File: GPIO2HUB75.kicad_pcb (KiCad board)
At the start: 2 copper layers, 30.2 x 59.5 mm, 7 parts, among them J2 Conn_02x20_Odd_Even_MountingP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, J3 Conn_02x08_Top_Bottom, J4 Conn_02x05_Odd_Even, J5 Conn_02x03_Odd_Even, M1 Fan_3pin

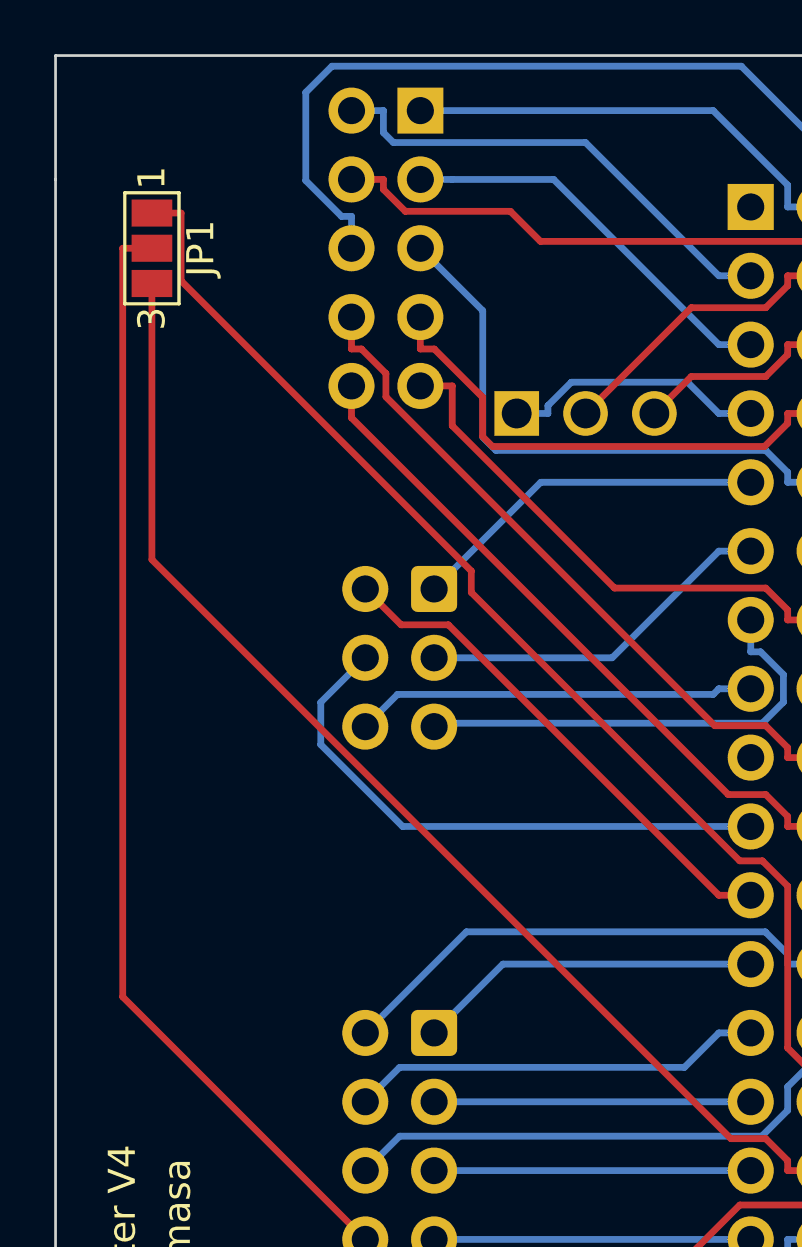
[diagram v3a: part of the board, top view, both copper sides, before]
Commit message: added tilt sensor
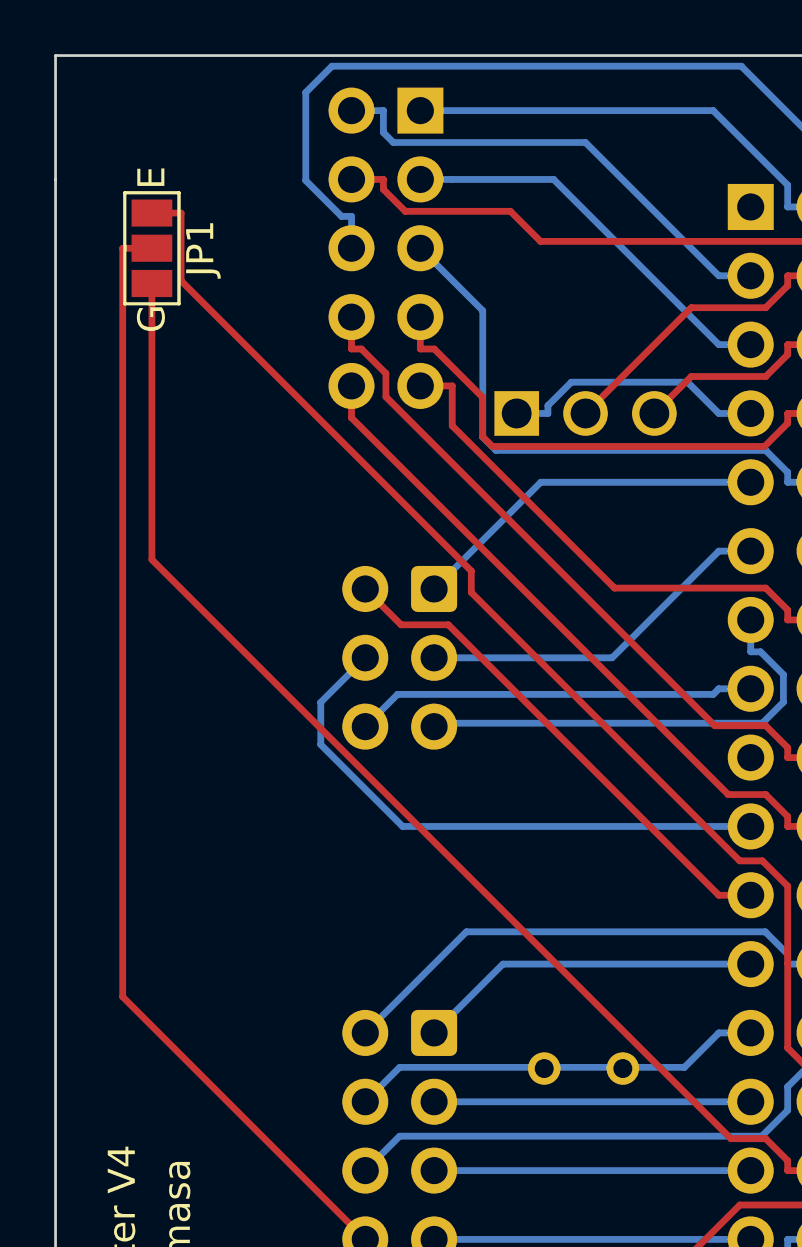
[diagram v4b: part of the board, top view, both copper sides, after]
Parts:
- added S1: CW1300-1, Tilt Sensor:CW13001, B.Cu at (156.8, 92.8)
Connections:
- J2 pad 1: unconnected-(J2-Pin_1-Pad1) -> Net-(J2-Pin_1)
- J2 pad 12: Net-(J2-Pin_12) -> unconnected-(J2-Pin_12-Pad12)
- J4 pad 2: Net-(J2-Pin_3) -> Net-(J2-Pin_1)
- J4 pad 4: Net-(J2-Pin_12) -> Net-(J2-Pin_3)
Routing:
- net Net-(J2-Pin_3): track 17.7 -> 49.1 mm
- net Net-(J2-Pin_12): track 31.3 -> 0.00 mm
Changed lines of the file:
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@@
   (net 2 "Net-(J2-Pin_39)")
   (net 3 "Net-(J2-Pin_7)")
-  (net 4 "unconnected-(J2-Pin_1-Pad1)")
+  (net 4 "Net-(J2-Pin_1)")
   (net 5 "Net-(J2-Pin_23)")
   (net 6 "Net-(J2-Pin_24)")
@@
   (net 27 "Net-(J2-Pin_10)")
   (net 28 "Net-(J2-Pin_11)")
-  (net 29 "Net-(J2-Pin_12)")
+  (net 29 "unconnected-(J2-Pin_12-Pad12)")
   (net 30 "Net-(J2-Pin_13)")
   (net 31 "Net-(J2-Pin_14)")
@@
   (net 40 "Net-(BZ1-+)")
   (net 41 "unconnected-(J2-Pin_17-Pad17)")
+  (net 42 "unconnected-(S1-Pad1)")
+  (net 43 "unconnected-(S1-Pad2)")
   (footprint "Jumper:SolderJumper-3_P1.3mm_Open_Pad1.0x1.5mm_NumberLabels" (layer "F.Cu")
     (at 139.446 62.484 -90)
@@
         (effects (font (size 1 1) (thickness 0.15)))
     )
-    (fp_text user "1" (at -2.6 0 90) (layer "F.SilkS")
+    (fp_text user "E" (at -2.6 0 90) (layer "F.SilkS")
         (effects (font (size 1 1) (thickness 0.15)))
     )
-    (fp_text user "3" (at 2.6 0 90) (layer "F.SilkS")
+    (fp_text user "G" (at 2.6 0 90) (layer "F.SilkS")
         (effects (font (size 1 1) (thickness 0.15)))
     )
@@
     (pad "3" smd rect (at 1.3 0 270) (size 1 1.5) (layers "F.Cu" "F.Mask")
       (net 38 "Net-(J2-Pin_30)") (pinfunction "B") (pintype "passive"))
+  )
+  (footprint "Tilt Sensor:CW13001" (layer "B.Cu")
+    (at 156.824 92.754 180)
+    (descr "CW1300-1-2")
+    (tags "Switch")
+    (property "Farnell Part Number" "")
+    (property "Farnell Price/Stock" "")
+    (property "Height" "10.2")
+    (property "Manufacturer_Name" "Assemtech")
+    (property "Manufacturer_Part_Number" "CW1300-1")
+    (property "Sheetfile" "GPIO2HUB75.kicad_sch")
+    (property "Sheetname" "")
+    (property "ki_description" "15 , 0.25 A, 60V, Non-Mercury Tilt Switch")
+    (attr through_hole)
+    (fp_text reference "S1" (at 0.575 0.425) (layer "B.SilkS")
+        (effects (font (size 1.27 1.27) (thickness 0.254)) (justify mirror))
+    )
+    (fp_text value "CW1300-1" (at 0.575 0.425) (layer "B.SilkS") hide
+        (effects (font (size 1.27 1.27) (thickness 0.254)) (justify mirror))
+    )
+    (fp_text user "${REFERENCE}" (at 0.575 0.425) (layer "B.Fab")
+        (effects (font (size 1.27 1.27) (thickness 0.254)) (justify mirror))
+    )
+    (fp_line (start 0 3.1) (end 0 3.1)
+      (stroke (width 0.2) (type solid)) (layer "B.SilkS"))
+    (fp_line (start 0 3.1) (end 0 3.1)
+      (stroke (width 0.2) (type solid)) (layer "B.SilkS"))
+    (fp_line (start 0 3.2) (end 0 3.2)
+      (stroke (width 0.2) (type solid)) (layer "B.SilkS"))
+    (fp_arc (start 0 3.1) (mid 0.05 3.15) (end 0 3.2)
+      (stroke (width 0.2) (type solid)) (layer "B.SilkS"))
+    (fp_arc (start 0 3.1) (mid 0.05 3.15) (end 0 3.2)
+      (stroke (width 0.2) (type solid)) (layer "B.SilkS"))
+    (fp_arc (start 0 3.2) (mid -0.05 3.15) (end 0 3.1)
+      (stroke (width 0.2) (type solid)) (layer "B.SilkS"))
+    (fp_line (start -3.35 -3.35) (end -3.35 4.2)
+      (stroke (width 0.1) (type solid)) (layer "B.CrtYd"))
+    (fp_line (start -3.35 4.2) (end 4.5 4.2)
+      (stroke (width 0.1) (type solid)) (layer "B.CrtYd"))
+    (fp_line (start 4.5 -3.35) (end -3.35 -3.35)
+      (stroke (width 0.1) (type solid)) (layer "B.CrtYd"))
+    (fp_line (start 4.5 4.2) (end 4.5 -3.35)
+      (stroke (width 0.1) (type solid)) (layer "B.CrtYd"))
+    (fp_line (start -2.35 0) (end -2.35 0)
+      (stroke (width 0.2) (type solid)) (layer "B.Fab"))
+    (fp_line (start 2.35 0) (end 2.35 0)
+      (stroke (width 0.2) (type solid)) (layer "B.Fab"))
+    (fp_arc (start -2.35 0) (mid 0 -2.35) (end 2.35 0)
+      (stroke (width 0.2) (type solid)) (layer "B.Fab"))
+    (fp_arc (start 2.35 0) (mid 0 2.35) (end -2.35 0)
+      (stroke (width 0.2) (type solid)) (layer "B.Fab"))
+    (pad "1" thru_hole circle (at 0 0 180) (size 1.2 1.2) (drill 0.7) (layers "*.Cu" "*.Mask")
+      (net 42 "unconnected-(S1-Pad1)") (pinfunction "1") (pintype "passive"))
+    (pad "2" thru_hole circle (at 2.9 0 180) (size 1.2 1.2) (drill 0.7) (layers "*.Cu" "*.Mask")
+      (net 43 "unconnected-(S1-Pad2)") (pinfunction "2") (pintype "passive"))
+    (model "C:/Users/Admin/Downloads/LIB_CW1300-1/CW1300-1/3D/CW1300-1.stp"
+      (offset (xyz 0 2.5 3))
+      (scale (xyz 1 1 1))
+      (rotate (xyz 90 0 0))
+    )
   )
   (footprint "Buzzer_Beeper:MagneticBuzzer_Kingstate_KCG0601" (layer "B.Cu")
@@
       (net 22 "Net-(J2-Pin_2)") (pinfunction "Pin_1") (pintype "passive"))
     (pad "2" thru_hole oval (at 2.54 0 180) (size 1.7 1.7) (drill 1) (layers "*.Cu" "*.Mask")
-      (net 23 "Net-(J2-Pin_3)") (pinfunction "Pin_2") (pintype "passive"))
+      (net 4 "Net-(J2-Pin_1)") (pinfunction "Pin_2") (pintype "passive"))
     (pad "3" thru_hole oval (at 0 -2.54 180) (size 1.7 1.7) (drill 1) (layers "*.Cu" "*.Mask")
       (net 24 "Net-(J2-Pin_5)") (pinfunction "Pin_3") (pintype "passive"))
     (pad "4" thru_hole oval (at 2.54 -2.54 180) (size 1.7 1.7) (drill 1) (layers "*.Cu" "*.Mask")
-      (net 29 "Net-(J2-Pin_12)") (pinfunction "Pin_4") (pintype "passive"))
+      (net 23 "Net-(J2-Pin_3)") (pinfunction "Pin_4") (pintype "passive"))
     (pad "5" thru_hole oval (at 0 -5.08 180) (size 1.7 1.7) (drill 1) (layers "*.Cu" "*.Mask")
       (net 27 "Net-(J2-Pin_10)") (pinfunction "Pin_5") (pintype "passive"))
@@
       (stroke (width 0.1) (type solid)) (layer "B.Fab"))
     (pad "1" thru_hole rect (at 0 0 180) (size 1.7 1.7) (drill 1) (layers "*.Cu" "*.Mask")
-      (net 4 "unconnected-(J2-Pin_1-Pad1)") (pinfunction "Pin_1") (pintype "passive"))
+      (net 4 "Net-(J2-Pin_1)") (pinfunction "Pin_1") (pintype "passive"))
     (pad "2" thru_hole oval (at -2.54 0 180) (size 1.7 1.7) (drill 1) (layers "*.Cu" "*.Mask")
       (net 22 "Net-(J2-Pin_2)") (pinfunction "Pin_2") (pintype "passive"))
@@
       (net 28 "Net-(J2-Pin_11)") (pinfunction "Pin_11") (pintype "passive"))
     (pad "12" thru_hole oval (at -2.54 -12.7 180) (size 1.7 1.7) (drill 1) (layers "*.Cu" "*.Mask")
-      (net 29 "Net-(J2-Pin_12)") (pinfunction "Pin_12") (pintype "passive"))
+      (net 29 "unconnected-(J2-Pin_12-Pad12)") (pinfunction "Pin_12") (pintype "passive"))
     (pad "13" thru_hole oval (at 0 -15.24 180) (size 1.7 1.7) (drill 1) (layers "*.Cu" "*.Mask")
       (net 30 "Net-(J2-Pin_13)") (pinfunction "Pin_13") (pintype "passive"))
@@
   (segment (start 160.1602 57.404) (end 162.9071 60.1509) (width 0.25) (layer "B.Cu") (net 22))
   (segment (start 164.084 60.96) (end 162.9071 60.96) (width 0.25) (layer "B.Cu") (net 22))
+  (segment (start 165.277 71.6559) (end 164.4498 72.4831) (width 0.25) (layer "F.Cu") (net 23))
+  (segment (start 148.7979 61.1209) (end 152.6768 61.1209) (width 0.25) (layer "F.Cu") (net 23))
+  (segment (start 146.812 59.944) (end 147.9889 59.944) (width 0.25) (layer "F.Cu") (net 23))
+  (segment (start 147.9889 60.3119) (end 148.7979 61.1209) (width 0.25) (layer "F.Cu") (net 23))
+  (segment (start 147.9889 59.944) (end 147.9889 60.3119) (width 0.25) (layer "F.Cu") (net 23))
+  (segment (start 164.4498 72.4831) (end 164.084 72.4831) (width 0.25) (layer "F.Cu") (net 23))
+  (segment (start 152.6768 61.1209) (end 153.7859 62.23) (width 0.25) (layer "F.Cu") (net 23))
+  (segment (start 165.277 62.9734) (end 165.277 71.6559) (width 0.25) (layer "F.Cu") (net 23))
+  (segment (start 164.084 73.66) (end 164.084 72.4831) (width 0.25) (layer "F.Cu") (net 23))
+  (segment (start 153.7859 62.23) (end 164.5336 62.23) (width 0.25) (layer "F.Cu") (net 23))
+  (segment (start 164.5336 62.23) (end 165.277 62.9734) (width 0.25) (layer "F.Cu") (net 23))
   (segment (start 161.544 63.5) (end 160.3671 63.5) (width 0.25) (layer "B.Cu") (net 23))
   (segment (start 147.9889 58.2132) (end 148.3566 58.5809) (width 0.25) (layer "B.Cu") (net 23))
@@
   (segment (start 161.544 73.66) (end 160.3671 73.66) (width 0.25) (layer "B.Cu") (net 28))
   (segment (start 149.86 77.597) (end 156.4301 77.597) (width 0.25) (layer "B.Cu") (net 28))
-  (segment (start 165.277 71.6559) (end 164.4498 72.4831) (width 0.25) (layer "F.Cu") (net 29))
-  (segment (start 148.7979 61.1209) (end 152.6768 61.1209) (width 0.25) (layer "F.Cu") (net 29))
-  (segment (start 146.812 59.944) (end 147.9889 59.944) (width 0.25) (layer "F.Cu") (net 29))
-  (segment (start 147.9889 60.3119) (end 148.7979 61.1209) (width 0.25) (layer "F.Cu") (net 29))
-  (segment (start 147.9889 59.944) (end 147.9889 60.3119) (width 0.25) (layer "F.Cu") (net 29))
-  (segment (start 164.4498 72.4831) (end 164.084 72.4831) (width 0.25) (layer "F.Cu") (net 29))
-  (segment (start 152.6768 61.1209) (end 153.7859 62.23) (width 0.25) (layer "F.Cu") (net 29))
-  (segment (start 165.277 62.9734) (end 165.277 71.6559) (width 0.25) (layer "F.Cu") (net 29))
-  (segment (start 164.084 73.66) (end 164.084 72.4831) (width 0.25) (layer "F.Cu") (net 29))
-  (segment (start 153.7859 62.23) (end 164.5336 62.23) (width 0.25) (layer "F.Cu") (net 29))
-  (segment (start 164.5336 62.23) (end 165.277 62.9734) (width 0.25) (layer "F.Cu") (net 29))
   (segment (start 162.7505 78.2176) (end 161.9098 77.3769) (width 0.25) (layer "B.Cu") (net 30))
   (segment (start 149.86 80.137) (end 149.987 80.01) (width 0.25) (layer "B.Cu") (net 30))

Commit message: version 5
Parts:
- removed J2: Conn_02x20_Odd_Even_MountingPin, Connector_PinSocket_2.54mm:PinSocket_2x20_P2.54mm_Vertical
- added RPiGPIO1: CONN_02X20, Connector_PinSocket_2.54mm:PinSocket_2x20_P2.54mm_Vertical, B.Cu at (164.0, 110.2)
- E: renamed from JP1; value SolderJumper_3_Open -> Data E
- GPIO1: renamed from J4; value Conn_02x05_Odd_Even -> 02x04; footprint Connector_PinHeader_2.54mm:PinHeader_2x05_P2.54mm_Horizontal -> Connector_PinHeader_2.54mm:PinHeader_2x04_P2.54mm_Horizontal
- HUB1: renamed from J3; value Conn_02x08_Top_Bottom -> Conn_02x08
- IO1: renamed from J5; value Conn_02x03_Odd_Even -> 02x03
- M1: value Fan_3pin -> Noctua
- S1: value CW1300-1 -> CW1300
- moved GPIO1 2.55 mm to (149.1, 59.9)
- moved M1 2.48 mm to (152.8, 71.1)
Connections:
- BZ1 pad 1: Net-(BZ1--) -> BUZZ
- E pad 1: Net-(J2-Pin_28) -> GPIO15
- E pad 3: Net-(J2-Pin_30) -> Net-(BZ1-+)
- GPIO1 pad 1: Net-(J2-Pin_2) -> GPIO 2
- GPIO1 pad 2: Net-(J2-Pin_1) -> GPIO 26
- GPIO1 pad 3: Net-(J2-Pin_5) -> GPIO 3
- GPIO1 pad 4: Net-(J2-Pin_3) -> GPIO 6
- GPIO1 pad 5: Net-(J2-Pin_10) -> GPIO 13
- GPIO1 pad 6: Net-(J2-Pin_16) -> VCC
- GPIO1 pad 7: Net-(J2-Pin_8) -> GPIO 19
- GPIO1 pad 8: Net-(J2-Pin_18) -> Net-(BZ1-+)
- HUB1 pad 1: Net-(J2-Pin_23) -> R1
- HUB1 pad 10: Net-(J2-Pin_32) -> B
- HUB1 pad 11: Net-(J2-Pin_35) -> C
- HUB1 pad 12: Net-(J2-Pin_36) -> D
- HUB1 pad 13: Net-(J2-Pin_37) -> Clock
- HUB1 pad 14: Net-(J2-Pin_38) -> Net-(BZ1-+)
- HUB1 pad 15: Net-(J2-Pin_40) -> OE-
- HUB1 pad 16: Net-(J2-Pin_39) -> Strobe
- HUB1 pad 2: Net-(J2-Pin_24) -> G1
- HUB1 pad 3: Net-(J2-Pin_27) -> B1
- HUB1 pad 4: Net-(J2-Pin_25) -> Net-(BZ1-+)
- HUB1 pad 5: Net-(J2-Pin_29) -> R2
- HUB1 pad 6: Net-(J2-Pin_26) -> G2
- HUB1 pad 7: Net-(J2-Pin_31) -> B2
- HUB1 pad 9: Net-(J2-Pin_33) -> A
- IO1 pad 1: Net-(J2-Pin_9) -> IO1
- IO1 pad 2: Net-(J2-Pin_21) -> IO2
- IO1 pad 3: Net-(J2-Pin_11) -> IO3
- IO1 pad 4: Net-(J2-Pin_19) -> IO4
- IO1 pad 5: Net-(J2-Pin_13) -> IO5
- IO1 pad 6: Net-(J2-Pin_15) -> Net-(BZ1-+)
- M1 pad 1: Net-(J2-Pin_7) -> VCC
- M1 pad 2: Net-(J2-Pin_4) -> Net-(BZ1-+)
- M1 pad 3: Net-(J2-Pin_6) -> FAN
- S1 pad 1: unconnected-(S1-Pad1) -> TILT
- S1 pad 2: unconnected-(S1-Pad2) -> Net-(BZ1-+)
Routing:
- net Net-(BZ1-+): track 17.6 -> 97.6 mm
- net GPIO 2: track 0.00 -> 62.5 mm
- net GPIO 3: track 0.00 -> 57.1 mm
- net VCC: track 0.00 -> 52.8 mm
- net Net-(J2-Pin_3): track 49.1 -> 0.00 mm
- net Net-(J2-Pin_16): track 48.9 -> 0.00 mm
- net Net-(J2-Pin_30): track 44.4 -> 0.00 mm
- net Net-(J2-Pin_28): track 44.3 -> 0.00 mm
- net BUZZ: track 0.00 -> 39.2 mm
- net C: track 0.00 -> 37.6 mm
- net G1: track 0.00 -> 36.7 mm
- net IO4: track 0.00 -> 34.1 mm
- net FAN: track 0.00 -> 33.2 mm
- net TILT: track 0.00 -> 32.5 mm
- net IO5: track 0.00 -> 32.2 mm
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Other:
- board size 30.2 x 59.5 mm -> 30.4 x 56.8 mm
- board text added: "RPiToHUB75 Adapter V5"
- board text removed: "RPiToHUB75 Adapter V4"
